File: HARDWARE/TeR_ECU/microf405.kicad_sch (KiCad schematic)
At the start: 24 parts, among them J1 FTSH-105-01-L-DV-K-TR, SW1 RST, U6 STM32F405VGTx, X2 ASE-xxxMHz

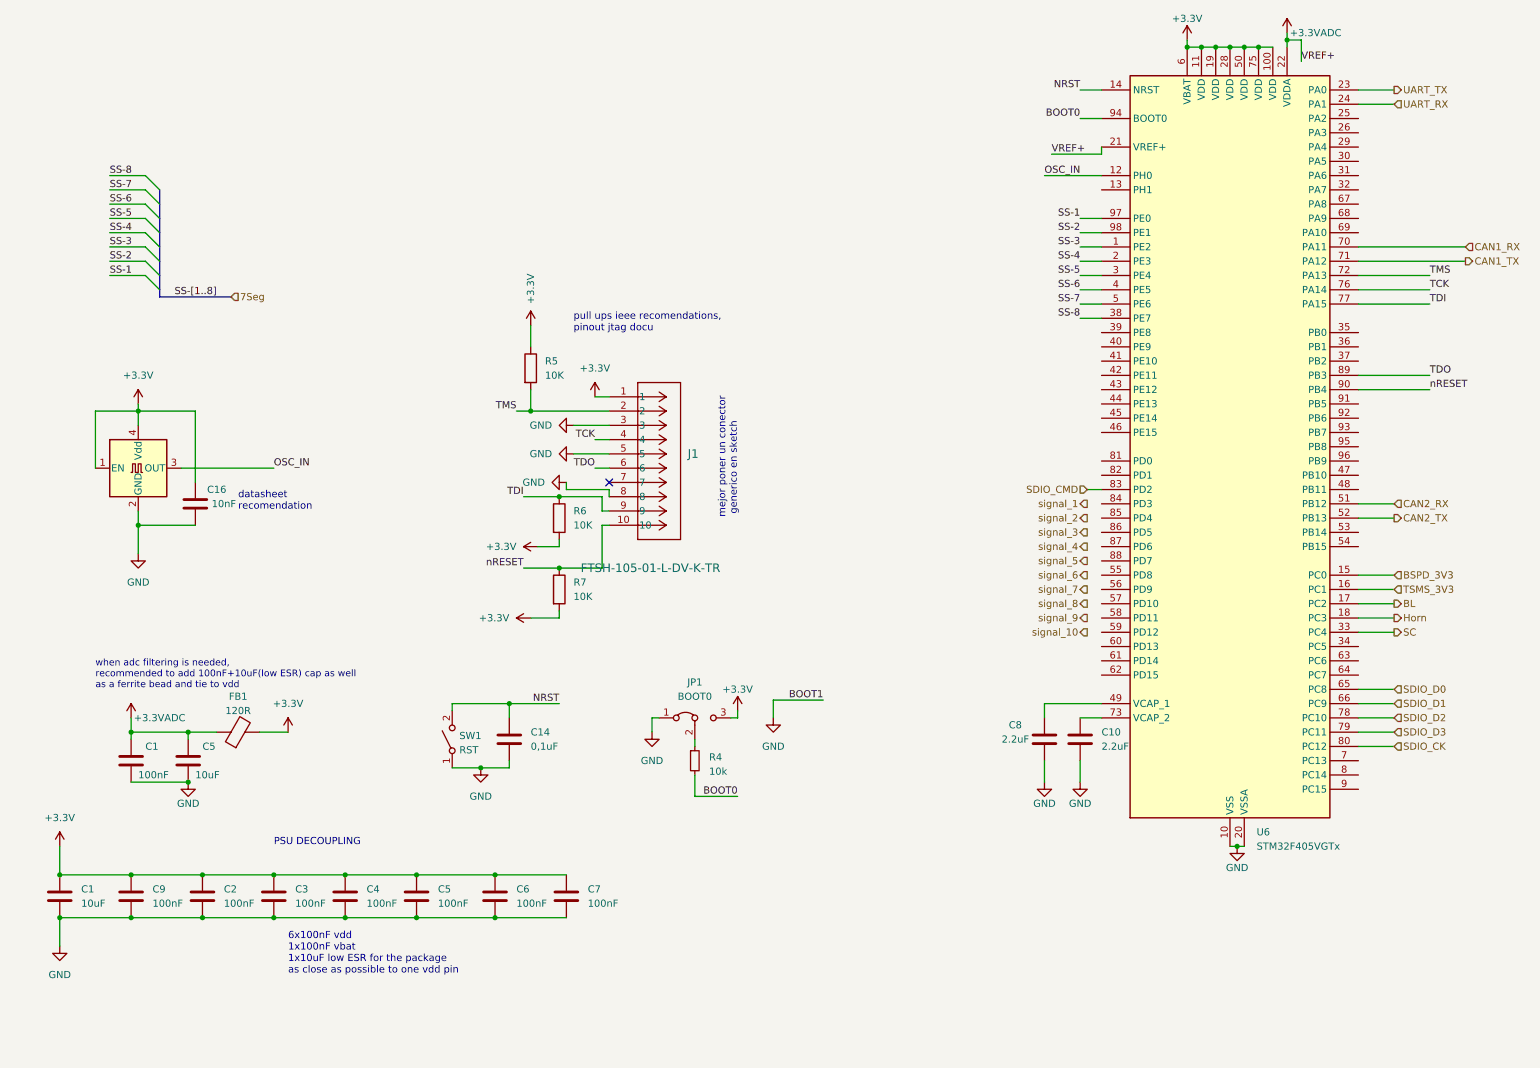
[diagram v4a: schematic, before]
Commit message: usb-c, good debug conn, switch
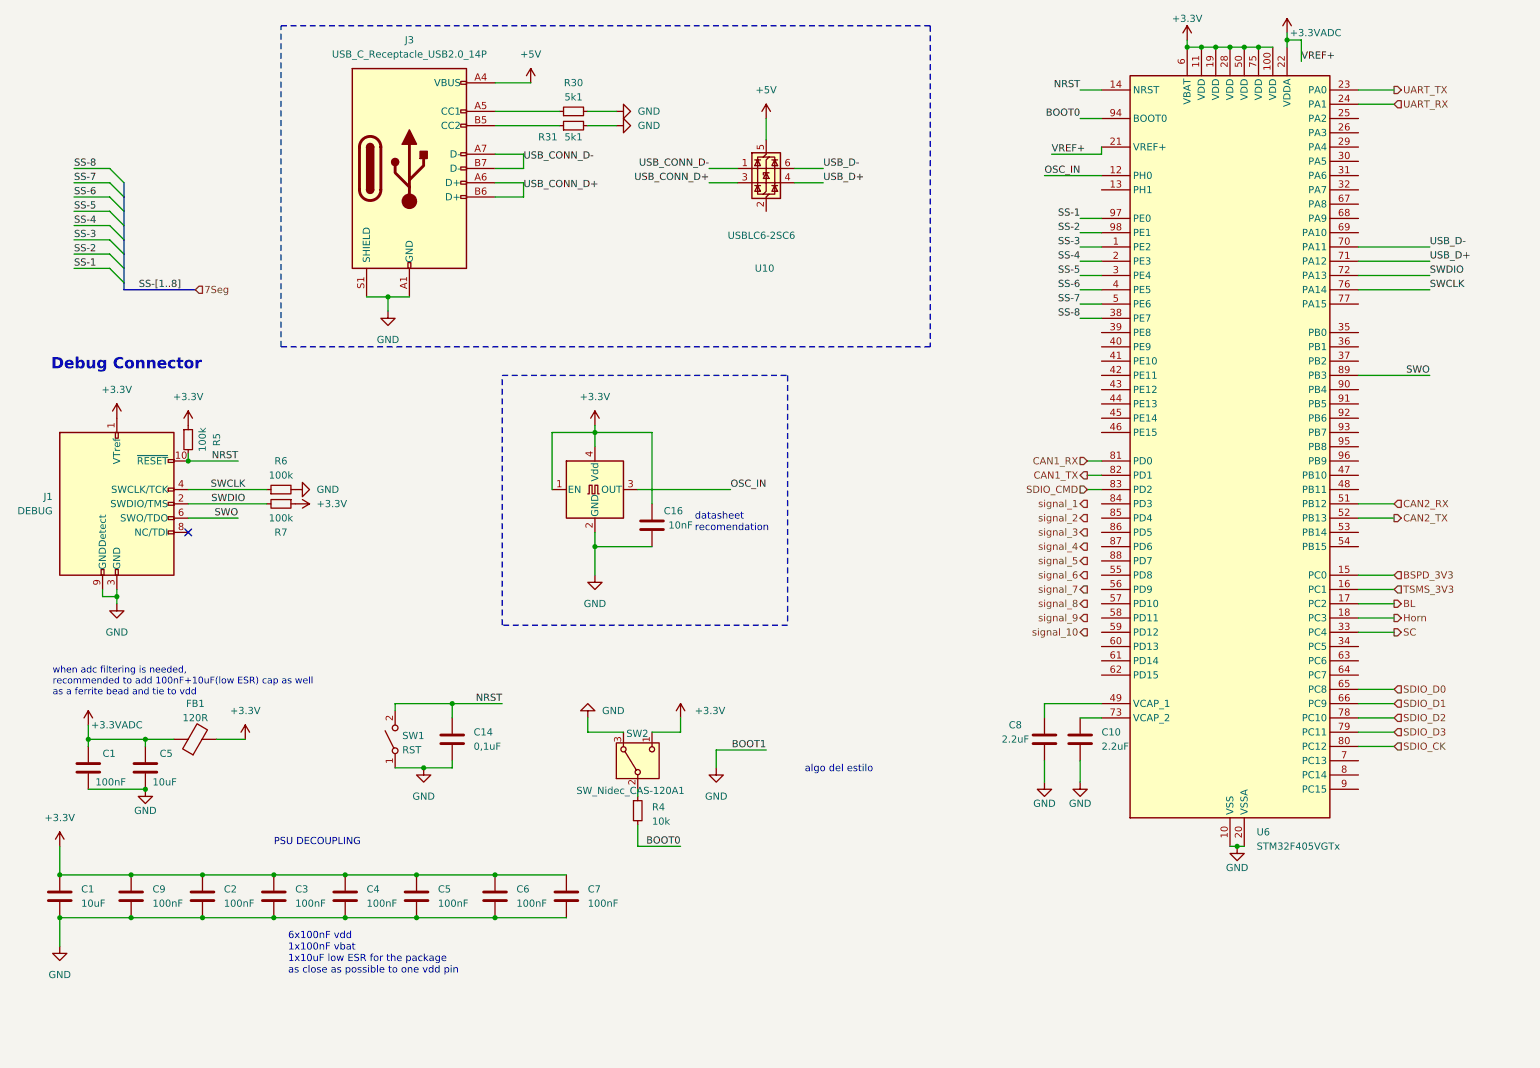
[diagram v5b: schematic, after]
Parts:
- removed J1: FTSH-105-01-L-DV-K-TR, CON10_2X5_DUK_FTSH_SAI, symbol 2024-04-21_17-21-18:FTSH-105-01-L-DV-K-TR
- removed JP1: BOOT0, Connector_PinHeader_2.00mm:PinHeader_1x03_P2.00mm_Vertical, symbol Jumper:Jumper_3_Bridged12
- removed R5, R6, R7: 10K, symbol Device:R
- added J1: DEBUG, Connector_PinHeader_1.27mm:PinHeader_2x05_P1.27mm_Vertical, symbol Connector:Conn_ARM_JTAG_SWD_10
- added J3: USB_C_Receptacle_USB2.0_14P, symbol Connector:USB_C_Receptacle_USB2.0_14P
- added R30, R31: 5k1, Resistor_SMD:R_0603_1608Metric, symbol Device:R_Small
- added R5, R6, R7: 100k, Resistor_SMD:R_0603_1608Metric, symbol Device:R_Small
- added SW2: SW_Nidec_CAS-120A1, Button_Switch_SMD:Nidec_Copal_CAS-120A, symbol Switch:SW_Nidec_CAS-120A1
- added U10: USBLC6-2SC6, Package_TO_SOT_SMD:SOT-23-6, symbol Power_Protection:USBLC6-2SC6
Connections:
- net +3.3V: now also J1.1 (VTref), R5.1, R7.1, SW2.1 (C)
- net CAN1_RX: now also U6.81 (PD0); no longer U6.70 (PA11)
- net CAN1_TX: now also U6.82 (PD1); no longer U6.71 (PA12)
- net GND: now also J1.3 (GND), J1.5 (GND), J1.9 (GNDDetect), J3.A1 (GND), J3.A12 (GND), J3.B1 (GND), J3.B12 (GND), J3.S1 (SHIELD), R30.2, R31.2, R6.2, SW2.3 (A)
- net NRST: now also J1.10 (~{RESET}), R5.2
- net at R4.1: now also SW2.2 (B)
- net TCK renamed SWCLK
- net SWCLK: now also J1.4 (SWCLK/TCK), R6.1
- net TDI: no longer names the net of U6.77 (PA15)
- net TDO renamed SWO
- net SWO: now also J1.6 (SWO/TDO)
- net TMS renamed SWDIO
- net SWDIO: now also J1.2 (SWDIO/TMS), R7.2
- net nRESET: no longer names the net of U6.90 (PB4)
- new net: J3.A5 (CC1), R30.1
- new net: J3.B5 (CC2), R31.1
- new net +5V: J3.A4 (VBUS), J3.A9 (VBUS), J3.B4 (VBUS), J3.B9 (VBUS), U10.5 (VBUS)
- new net USB_CONN_D+: J3.A6 (D+), J3.B6 (D+), U10.3 (I/O2)
- new net USB_CONN_D-: J3.A7 (D-), J3.B7 (D-), U10.1 (I/O1)
- new net USB_D+: U10.4 (I/O2), U6.71 (PA12)
- new net USB_D-: U10.6 (I/O1), U6.70 (PA11)
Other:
- note added: "Debug Connector"
- note added: "algo del estilo"
- note removed: "mejor poner un conector generico en sketch"
- note removed: "pull ups ieee recomendations, pinout jtag docu"
- moved on the sheet: C1, C14, C16, C5, FB1, R4, SW1

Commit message: Kept improving schmatic for V2
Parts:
- removed J3: USB_C_Receptacle_USB2.0_14P, symbol Connector:USB_C_Receptacle_USB2.0_14P
- removed R30, R31: 5k1, Resistor_SMD:R_0603_1608Metric, symbol Device:R_Small
- removed R4: 10k, Resistor_SMD:R_0603_1608Metric, symbol Device:R_Small
- removed SW2: SW_Nidec_CAS-120A1, Button_Switch_SMD:Nidec_Copal_CAS-120A, symbol Switch:SW_Nidec_CAS-120A1
- removed U10: USBLC6-2SC6, Package_TO_SOT_SMD:SOT-23-6, symbol Power_Protection:USBLC6-2SC6
- added R33: 10k, Resistor_SMD:R_0603_1608Metric, symbol Device:R_Small
- added SW3: BOOT0, Button_Switch_SMD:SW_Tactile_SPST_NO_Straight_CK_PTS636Sx25SMTRLFS, symbol Switch:SW_SPST
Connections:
- net +3.3V: now also SW3.1 (A)
- net +3.3VADC: no longer U6.21 (VREF+)
- net BOOT0: now also R33.1, SW3.2 (B)
- net GND: now also R33.2
- new net VREF+: U6.21 (VREF+)
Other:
- note added: "ADC SUPPLY"
- note added: "BOOT"
- note added: "HSE"
- note added: "RST"
- note removed: "algo del estilo"
- moved on the sheet: C1, C14, C16, C2, C3, C4, C5, C6, C7, C9, FB1, J1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

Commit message: Quick changes
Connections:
- net SS-1: no longer names the net of U6.97 (PE0)
- net SS-2: no longer names the net of U6.98 (PE1)
- net SS-3: no longer names the net of U6.1 (PE2)
- net SS-4: no longer names the net of U6.2 (PE3)
- net SS-5: no longer names the net of U6.3 (PE4)
- net SS-6: no longer names the net of U6.4 (PE5)
- net SS-7: no longer names the net of U6.5 (PE6)
- net SS-8: no longer names the net of U6.38 (PE7)
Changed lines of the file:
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@@
-	(wire
-		(pts
-			(xy 205.74 55.88) (xy 209.55 55.88)
-		)
-		(stroke
-			(width 0)
-			(type default)
-		)
-	)
 	(wire
 		(pts
@@
 	(wire
 		(pts
-			(xy 205.74 60.96) (xy 209.55 60.96)
-		)
-		(stroke
-			(width 0)
-			(type default)
-		)
-	)
-	(wire
-		(pts
 			(xy 255.27 114.3) (xy 261.62 114.3)
 		)
@@
 	(wire
 		(pts
-			(xy 205.74 50.8) (xy 209.55 50.8)
-		)
-		(stroke
-			(width 0)
-			(type default)
-		)
-	)
-	(wire
-		(pts
 			(xy 36.83 156.21) (xy 31.75 156.21)
 		)
@@
 	(wire
 		(pts
-			(xy 205.74 53.34) (xy 209.55 53.34)
-		)
-		(stroke
-			(width 0)
-			(type default)
-		)
-	)
-	(wire
-		(pts
 			(xy 139.7 185.42) (xy 153.67 185.42)
 		)
@@
 	(wire
 		(pts
-			(xy 205.74 63.5) (xy 209.55 63.5)
-		)
-		(stroke
-			(width 0)
-			(type default)
-		)
-	)
-	(wire
-		(pts
 			(xy 205.74 137.16) (xy 209.55 137.16)
 		)
@@
 	(wire
 		(pts
-			(xy 205.74 48.26) (xy 209.55 48.26)
-		)
-		(stroke
-			(width 0)
-			(type default)
-		)
-	)
-	(wire
-		(pts
 			(xy 255.27 58.42) (xy 267.97 58.42)
 		)
@@
 	(wire
 		(pts
-			(xy 205.74 66.04) (xy 209.55 66.04)
-		)
-		(stroke
-			(width 0)
-			(type default)
-		)
-	)
-	(wire
-		(pts
 			(xy 24.13 175.26) (xy 24.13 177.8)
 		)
@@
 		(pts
 			(xy 76.2 185.42) (xy 88.9 185.42)
-		)
-		(stroke
-			(width 0)
-			(type default)
-		)
-	)
-	(wire
-		(pts
-			(xy 205.74 58.42) (xy 209.55 58.42)
 		)
 		(stroke
@@
 		)
 	)
-	(label "SS-2"
-		(at 205.74 50.8 180)
-		(fields_autoplaced yes)
-		(effects
-			(font
-				(size 1.27 1.27)
-			)
-			(justify right bottom)
-		)
-	)
 	(label "SWDIO"
 		(at 58.42 43.18 180)
@@
 		)
 	)
-	(label "SS-5"
-		(at 205.74 58.42 180)
-		(fields_autoplaced yes)
-		(effects
-			(font
-				(size 1.27 1.27)
-			)
-			(justify right bottom)
-		)
-	)
 	(label "SWO"
 		(at 57.15 45.72 180)
@@
 		)
 	)
-	(label "SS-6"
-		(at 205.74 60.96 180)
-		(fields_autoplaced yes)
-		(effects
-			(font
-				(size 1.27 1.27)
-			)
-			(justify right bottom)
-		)
-	)
-	(label "SS-1"
-		(at 205.74 48.26 180)
-		(fields_autoplaced yes)
-		(effects
-			(font
-				(size 1.27 1.27)
-			)
-			(justify right bottom)
-		)
-	)
-	(label "SS-7"
-		(at 205.74 63.5 180)
-		(fields_autoplaced yes)
-		(effects
-			(font
-				(size 1.27 1.27)
-			)
-			(justify right bottom)
-		)
-	)
-	(label "SS-8"
-		(at 205.74 66.04 180)
-		(fields_autoplaced yes)
-		(effects
-			(font
-				(size 1.27 1.27)
-			)
-			(justify right bottom)
-		)
-	)
-	(label "SS-4"
-		(at 205.74 55.88 180)
-		(fields_autoplaced yes)
-		(effects
-			(font
-				(size 1.27 1.27)
-			)
-			(justify right bottom)
-		)
-	)
 	(label "NRST"
 		(at 57.15 35.56 180)
@@
 		(fields_autoplaced yes)
 		(effects
-			(font
-				(size 1.27 1.27)
-			)
-			(justify right bottom)
-		)
-	)
-	(label "SS-3"
-		(at 205.74 53.34 180)
-		(fields_autoplaced yes)
-		(effects
